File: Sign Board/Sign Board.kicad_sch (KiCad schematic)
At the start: 17 parts, among them J1 Conn_01x03_Socket, J2 Conn_01x03_Pin, J3 Conn_01x03_Pin, J4 Conn_01x03_Pin, J5 Conn_01x03_Pin, J6 Conn_01x03_Pin

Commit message: Break Everything
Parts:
- removed F6: Fuse, Fuse:Fuseholder_Blade_Mini_Keystone_3568, symbol Device:Fuse
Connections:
- net at F1.1, F2.1, F3.1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: now also J1.3 (Pin_3)
- net at J2.3 (Pin_3): now also J1.1 (Pin_1); no longer J1.3 (Pin_3)
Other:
- moved on the sheet: J1
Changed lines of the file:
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@@
-	(wire
-		(pts
-			(xy 63.5 71.12) (xy 63.5 76.2)
-		)
-		(stroke
-			(width 0)
-			(type default)
-		)
-	)
 	(wire
 		(pts
@@
 	(wire
 		(pts
+			(xy 63.5 58.42) (xy 63.5 76.2)
+		)
+		(stroke
+			(width 0)
+			(type default)
+		)
+	)
+	(wire
+		(pts
 			(xy 88.9 111.76) (xy 88.9 124.46)
 		)
@@
 		(pts
 			(xy 101.6 124.46) (xy 114.3 124.46)
-		)
-		(stroke
-			(width 0)
-			(type default)
-		)
-	)
-	(wire
-		(pts
-			(xy 63.5 58.42) (xy 63.5 63.5)
 		)
 		(stroke
@@
 	(symbol
 		(lib_id "Connector:Conn_01x03_Socket")
-		(at 45.72 55.88 180)
-		(unit 1)
-		(exclude_from_sim no)
-		(in_bom yes)
-		(on_board yes)
-		(dnp no)
-		(fields_autoplaced yes)
+		(at 45.72 55.88 0)
+		(mirror y)
+		(unit 1)
+		(exclude_from_sim no)
+		(in_bom yes)
+		(on_board yes)
+		(dnp no)
 		(property "Reference" "J1"
-			(at 46.355 48.26 0)
+			(at 46.355 63.5 0)
 			(effects
 				(font
@@
 		)
 		(property "Value" "Conn_01x03_Socket"
-			(at 46.355 50.8 0)
+			(at 46.355 60.96 0)
 			(effects
 				(font
@@
 					(unit 1)
 				)
-			)
-		)
-	)
-	(symbol
-		(lib_id "Device:Fuse")
-		(at 63.5 67.31 180)
-		(unit 1)
-		(exclude_from_sim no)
-		(in_bom yes)
-		(on_board yes)
-		(dnp no)
-		(fields_autoplaced yes)
-		(property "Reference" "F6"
-			(at 66.04 66.0399 0)
-			(effects
-				(font
-					(size 1.27 1.27)
-				)
-				(justify right)
-			)
-		)
-		(property "Value" "Fuse"
-			(at 66.04 68.5799 0)
-			(effects
-				(font
-					(size 1.27 1.27)
-				)
-				(justify right)
-			)
-		)
-		(property "Footprint" "Fuse:Fuseholder_Blade_Mini_Keystone_3568"
-			(at 65.278 67.31 90)
-			(effects
-				(font
-					(size 1.27 1.27)
-				)
-				(hide yes)
-			)
-		)
-		(property "Datasheet" "~"
-			(at 63.5 67.31 0)
-			(effects
-				(font
-					(size 1.27 1.27)
-				)
-				(hide yes)
-			)
-		)
-		(property "Description" "Fuse"
-			(at 63.5 67.31 0)
-			(effects
-				(font
-					(size 1.27 1.27)
-				)
-				(hide yes)
-			)
-		)
-		(pin "2"
-		)
-		(pin "1"
-		)
-		(instances
-			(project "Sign Board"
-				(path "/4e28a67c-3cb0-46df-9cc0-96316a654950"
-					(reference "F6")
-					(unit 1)
-				)

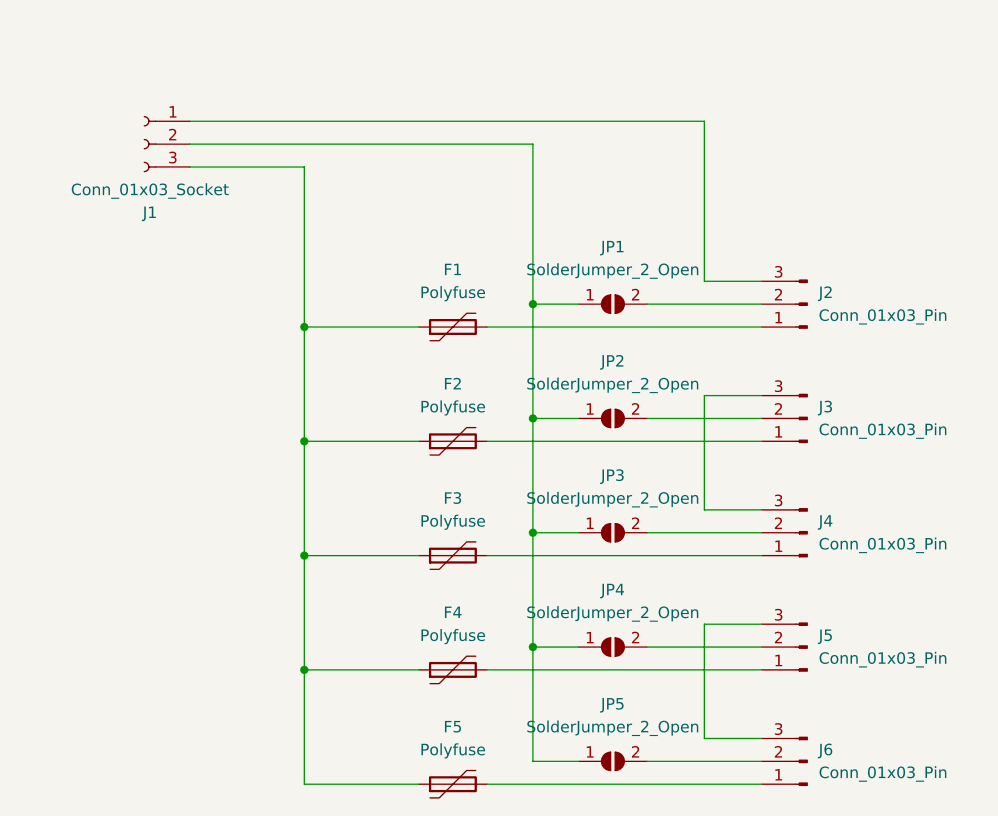
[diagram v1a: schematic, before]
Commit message: Reworked GND/Power planes and adjusted schematic to match application
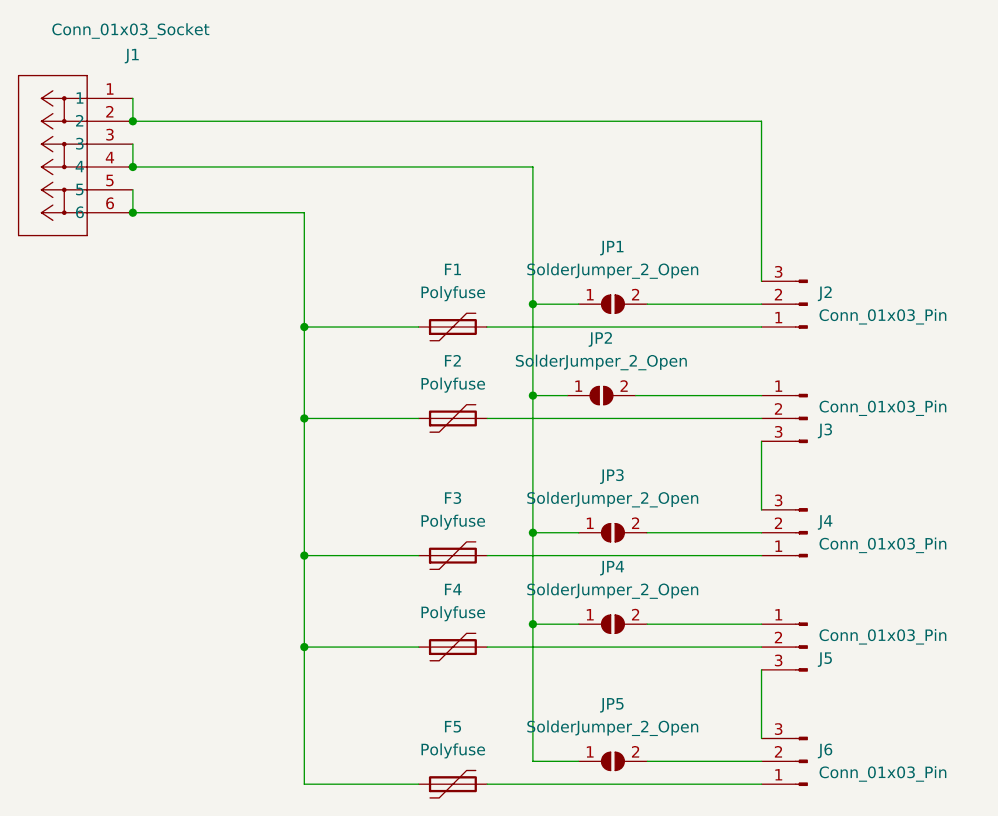
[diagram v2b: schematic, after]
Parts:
- J1: footprint TerminalBlock_Phoenix:TerminalBlock_Phoenix_MKDS-3-3-5.08_1x03_P5.08mm_Horizontal -> CONN_1017492; symbol Connector:Conn_01x03_Socket -> 2024-08-24_05-43-39:1017504
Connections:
- net at F1.1, F2.1, F3.1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: now also J1.5, J1.6; no longer J1.3 (Pin_3)
- net at JP1.1 (A), JP2.1 (A), JP3.1 (A)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: now also J1.3, J1.4; no longer J1.2 (Pin_2)
- net at J5.1 (Pin_1): now also JP4.2 (B); no longer F4.2
- net at J5.2 (Pin_2): now also F4.2; no longer JP4.2 (B)
- net at J1.1, J2.3 (Pin_3): now also J1.2
- net at F2.2: now also J3.2 (Pin_2); no longer J3.1 (Pin_1)
- net at JP2.2 (B): now also J3.1 (Pin_1); no longer J3.2 (Pin_2)
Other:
- moved on the sheet: F2, F4, J3, J5, JP2, JP4
